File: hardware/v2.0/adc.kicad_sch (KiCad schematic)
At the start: 18 parts, among them IC2 LTC2256CUJ-12#PBF, J7 RSP-122811-01, U1 ECP5U-25F-CABGA256, U11 LT1993CUD-2_PBF, Y2 SG-8018CG 50.000000MHz

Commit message: ADC SPI SDO
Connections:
- net SDI: now also U1.E13 (PT62B/-); no longer U1.E12 (PT58B/-)
- net SENSE: now also U1.E12 (PT58B/-); no longer U1.E13 (PT62B/-)
- net ~{CS}: now also U1.C12 (PT56B/-); no longer U1.D13 (PT62A/+)
- net SDO: now reaches IC2.16 (SDO)
- net SDO: now also U1.D13 (PT62A/+)
- no-connect marks 5 -> 4
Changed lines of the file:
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@@
-	)
-	(no_connect
-		(at 149.86 135.89)
 	)
 	(no_connect
@@
 	(wire
 		(pts
+			(xy 149.86 135.89) (xy 149.86 142.24)
+		)
+		(stroke
+			(width 0)
+			(type default)
+		)
+	)
+	(wire
+		(pts
 			(xy 106.68 101.6) (xy 106.68 100.33)
 		)
@@
 		(pts
 			(xy 248.92 116.84) (xy 258.572 116.84)
+		)
+		(stroke
+			(width 0)
+			(type default)
+		)
+	)
+	(wire
+		(pts
+			(xy 248.92 109.22) (xy 258.572 109.22)
 		)
 		(stroke
@@
 		)
 	)
-	(label "~{CS}"
-		(at 251.46 104.14 0)
-		(effects
-			(font
-				(size 1.27 1.27)
-			)
-			(justify left bottom)
-		)
-	)
 	(label "D0_1+"
 		(at 167.64 88.9 0)
@@
 		)
 	)
+	(label "~{CS}"
+		(at 251.46 109.22 0)
+		(effects
+			(font
+				(size 1.27 1.27)
+			)
+			(justify left bottom)
+		)
+	)
 	(label "CLKOUT+"
 		(at 259.588 86.36 180)
@@
 		)
 	)
+	(label "SDO"
+		(at 149.86 135.89 270)
+		(effects
+			(font
+				(size 1.27 1.27)
+			)
+			(justify right bottom)
+		)
+	)
 	(label "SENSE"
 		(at 134.62 71.12 180)
@@
 		)
 	)
+	(label "SDO"
+		(at 251.46 104.14 0)
+		(effects
+			(font
+				(size 1.27 1.27)
+			)
+			(justify left bottom)
+		)
+	)

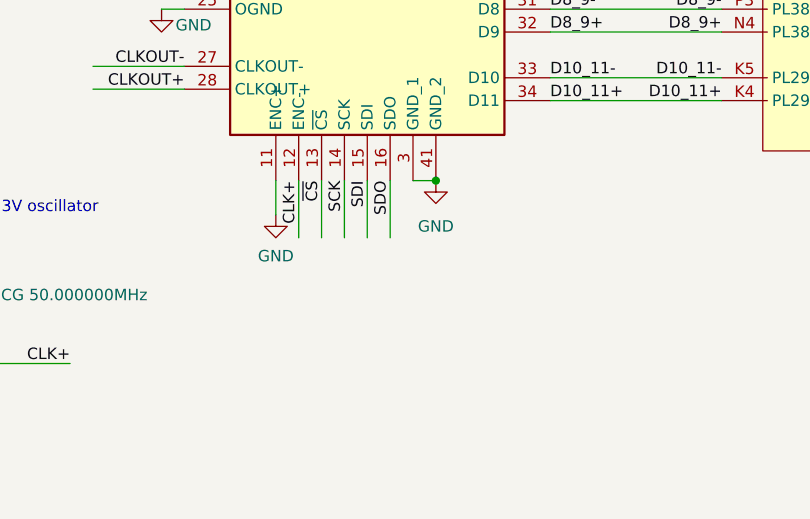
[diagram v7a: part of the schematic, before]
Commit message: ADC SPI SDO pull up
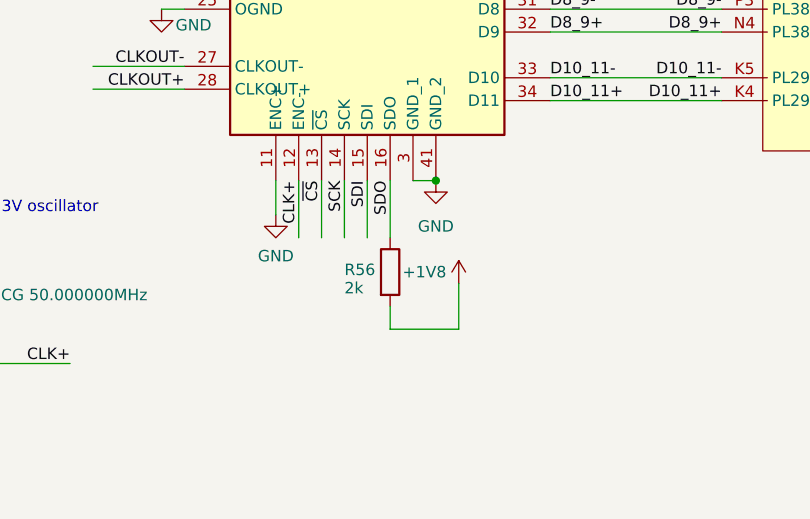
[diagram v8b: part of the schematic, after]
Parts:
- added R56: 2k, Resistor_SMD:R_0402_1005Metric, symbol Device:R
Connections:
- net +1V8: now also R56.2
- net SDO: now also R56.1
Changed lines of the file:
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@@
 	(wire
 		(pts
+			(xy 149.86 149.86) (xy 149.86 152.4)
+		)
+		(stroke
+			(width 0)
+			(type default)
+		)
+	)
+	(wire
+		(pts
 			(xy 78.74 153.67) (xy 78.74 148.59)
 		)
@@
 	(wire
 		(pts
+			(xy 157.48 147.32) (xy 157.48 152.4)
+		)
+		(stroke
+			(width 0)
+			(type default)
+		)
+	)
+	(wire
+		(pts
 			(xy 167.64 96.52) (xy 186.69 96.52)
 		)
@@
 	(wire
 		(pts
+			(xy 149.86 152.4) (xy 157.48 152.4)
+		)
+		(stroke
+			(width 0)
+			(type default)
+		)
+	)
+	(wire
+		(pts
 			(xy 139.7 77.47) (xy 142.24 77.47)
 		)
@@
 	)
 	(symbol
+		(lib_id "power:+3V3")
+		(at 157.48 147.32 0)
+		(unit 1)
+		(exclude_from_sim no)
+		(in_bom yes)
+		(on_board yes)
+		(dnp no)
+		(property "Reference" "#PWR0143"
+			(at 157.48 151.13 0)
+			(effects
+				(font
+					(size 1.27 1.27)
+				)
+				(hide yes)
+			)
+		)
+		(property "Value" "+1V8"
+			(at 153.67 146.05 0)
+			(effects
+				(font
+					(size 1.27 1.27)
+				)
+			)
+		)
+		(property "Footprint" ""
+			(at 157.48 147.32 0)
+			(effects
+				(font
+					(size 1.27 1.27)
+				)
+				(hide yes)
+			)
+		)
+		(property "Datasheet" ""
+			(at 157.48 147.32 0)
+			(effects
+				(font
+					(size 1.27 1.27)
+				)
+				(hide yes)
+			)
+		)
+		(property "Description" "Power symbol creates a global label with name \"+3V3\""
+			(at 157.48 147.32 0)
+			(effects
+				(font
+					(size 1.27 1.27)
+				)
+				(hide yes)
+			)
+		)
+		(pin "1"
+		)
+		(instances
+			(project "icepi-zero"
+				(path "/f88da08e-cf42-4d03-a08f-3f602fe6658d/b5a9aa02-311b-4a9a-a7d4-646f15cdd9c2"
+					(reference "#PWR0143")
+					(unit 1)
+				)
+			)
+		)
+	)
+	(symbol
 		(lib_id "Device:C_Small")
 		(at 121.92 104.14 0)
@@
 					(unit 1)
 				)
+			)
+		)
+	)
+	(symbol
+		(lib_id "Device:R")
+		(at 149.86 146.05 0)
+		(unit 1)
+		(exclude_from_sim no)
+		(in_bom yes)
+		(on_board yes)
+		(dnp no)
+		(property "Reference" "R56"
+			(at 144.78 145.796 0)
+			(effects
+				(font
+					(size 1.27 1.27)
+				)
+				(justify left)
+			)
+		)
+		(property "Value" "2k"
+			(at 144.78 147.828 0)
+			(effects
+				(font
+					(size 1.27 1.27)
+				)
+				(justify left)
+			)
+		)
+		(property "Footprint" "Resistor_SMD:R_0402_1005Metric"
+			(at 148.082 146.05 90)
+			(effects
+				(font
+					(size 1.27 1.27)
+				)
+				(hide yes)
+			)
+		)
+		(property "Datasheet" "~"
+			(at 149.86 146.05 0)
+			(effects
+				(font
+					(size 1.27 1.27)
+				)
+				(hide yes)
+			)
+		)
+		(property "Description" "Resistor"
+			(at 149.86 146.05 0)
+			(effects
+				(font
+					(size 1.27 1.27)
+				)
+				(hide yes)
+			)
+		)
+		(property "LCSC Part #" "C11702"
+			(at 149.86 146.05 0)
+			(effects
+				(font
+					(size 1.27 1.27)
+				)
+				(hide yes)
+			)
+		)
+		(property "LCSC Link" "https://www.lcsc.com/product-detail/C4109.html"
+			(at 149.86 146.05 0)
+			(effects
+				(font
+					(size 1.27 1.27)
+				)
+				(hide yes)
+			)
+		)
+		(property "Manufactuer Part Number" "0402WGF2001TCE"
+			(at 149.86 146.05 0)
+			(effects
+				(font
+					(size 1.27 1.27)
+				)
+				(hide yes)
+			)
+		)
+		(property "Note" ""
+			(at 149.86 146.05 0)
+			(effects
+				(font
+					(size 1.27 1.27)
+				)
+				(hide yes)
+			)
+		)
+		(property "Notes" ""
+			(at 149.86 146.05 0)
+			(effects
+				(font
+					(size 1.27 1.27)
+				)
+				(hide yes)
+			)
+		)
+		(pin "1"
+		)
+		(pin "2"
+		)
+		(instances
+			(project "icepi-zero"
+				(path "/f88da08e-cf42-4d03-a08f-3f602fe6658d/b5a9aa02-311b-4a9a-a7d4-646f15cdd9c2"
+					(reference "R56")
+					(unit 1)
+				)
